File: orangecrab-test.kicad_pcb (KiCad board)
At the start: 2 copper layers, 45.7 x 58.4 mm, 27 parts, among them J1 Conn_01x16, J2 Conn_01x12, SW1 SW_Push, U1 DAC53608RTET, U2 MCP23S08T-E-ML

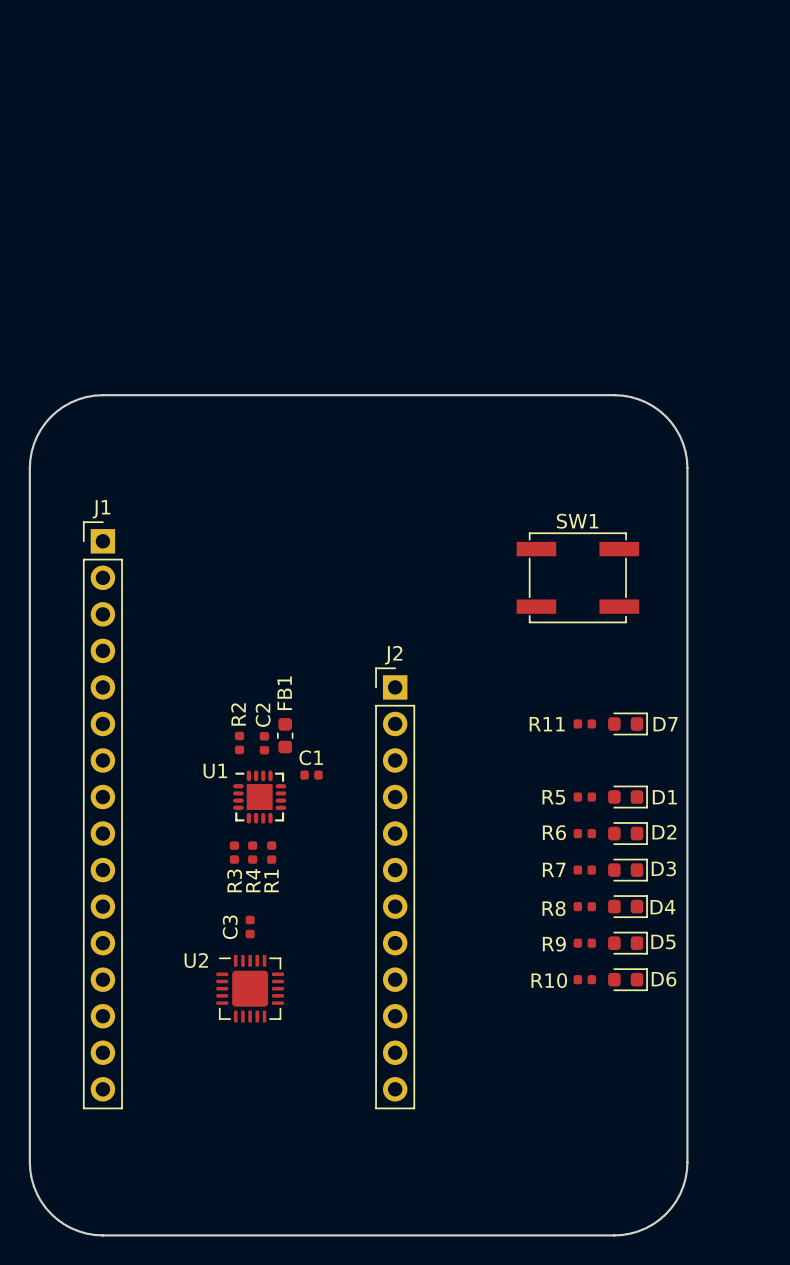
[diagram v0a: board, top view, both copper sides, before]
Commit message: Add FTDI from programming the initial firmware
Signed-off-by: Michael Welling <mwelling@ieee.org>
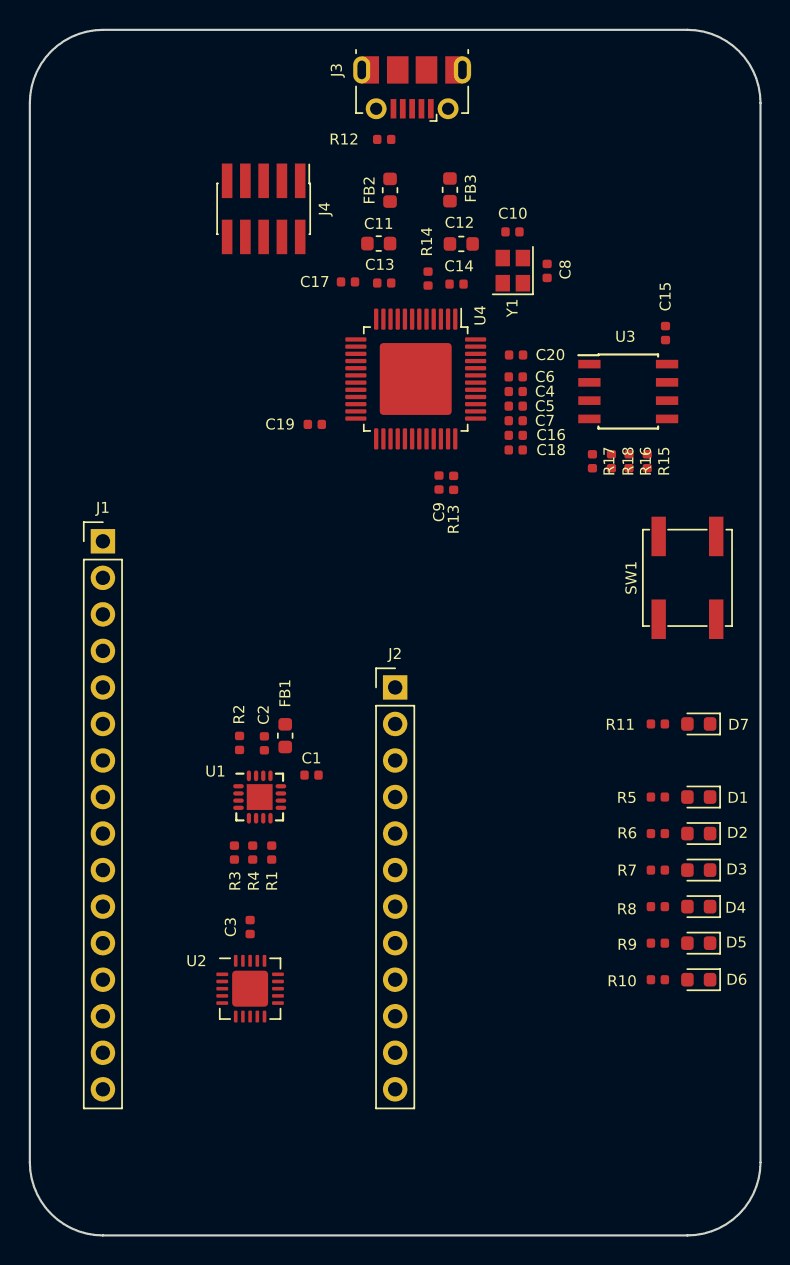
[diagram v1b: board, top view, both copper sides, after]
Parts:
- added C10: 10pF, Capacitor_SMD:C_0402_1005Metric, F.Cu at (130.1, 42.0)
- added C11: 4.7uF, Capacitor_SMD:C_0603_1608Metric, F.Cu at (120.8, 42.8)
- added C12: 4.7uF, Capacitor_SMD:C_0603_1608Metric, F.Cu at (126.5, 42.8)
- added C13: .1uF, Capacitor_SMD:C_0402_1005Metric, F.Cu at (121.2, 45.5)
- added C14: .1uF, Capacitor_SMD:C_0402_1005Metric, F.Cu at (126.2, 45.6)
- added C15: .1uF, Capacitor_SMD:C_0402_1005Metric, F.Cu at (140.7, 49.0)
- added C16: .1uF, Capacitor_SMD:C_0402_1005Metric, F.Cu at (130.3, 56.1)
- added C17: .1uF, Capacitor_SMD:C_0402_1005Metric, F.Cu at (118.6, 45.5)
- added C18: .1uF, Capacitor_SMD:C_0402_1005Metric, F.Cu at (130.3, 57.1)
- added C19: .1uF, Capacitor_SMD:C_0402_1005Metric, F.Cu at (116.3, 55.4)
- added C20: .1uF, Capacitor_SMD:C_0402_1005Metric, F.Cu at (130.3, 50.5)
- added C4: 4.7uF, Capacitor_SMD:C_0402_1005Metric, F.Cu at (130.3, 53.1)
- added C5: 4.7uF, Capacitor_SMD:C_0402_1005Metric, F.Cu at (130.3, 54.1)
- added C6: .1uF, Capacitor_SMD:C_0402_1005Metric, F.Cu at (130.3, 52.1)
- added C7: .1uF, Capacitor_SMD:C_0402_1005Metric, F.Cu at (130.3, 55.1)
- added C8: 10pF, Capacitor_SMD:C_0402_1005Metric, F.Cu at (132.5, 44.7)
- added C9: 10nF, Capacitor_SMD:C_0402_1005Metric, F.Cu at (125.0, 59.4)
- added FB2: Ferrite_Bead_Small, Inductor_SMD:L_0603_1608Metric, F.Cu at (121.6, 39.1)
- added FB3: Ferrite_Bead_Small, Inductor_SMD:L_0603_1608Metric, F.Cu at (125.7, 39.1)
- added J3: USB_B_Micro, Connector_USB:USB_Micro-B_Molex-105017-0001, F.Cu at (123.1, 32.0)
- added J4: JTAG, Connector_PinHeader_1.27mm:PinHeader_2x05_P1.27mm_Vertical_SMD, F.Cu at (112.8, 40.4)
- added R12: 1M, Resistor_SMD:R_0402_1005Metric, F.Cu at (121.2, 35.6)
- added R13: 4.7K, Resistor_SMD:R_0402_1005Metric, F.Cu at (126.0, 59.4)
- added R14: 12K, Resistor_SMD:R_0402_1005Metric, F.Cu at (124.2, 45.2)
- added R15: 4.7K, Resistor_SMD:R_0402_1005Metric, F.Cu at (139.4, 57.9)
- added R16: 4.7K, Resistor_SMD:R_0402_1005Metric, F.Cu at (138.2, 57.9)
- added R17: 2.2K, Resistor_SMD:R_0402_1005Metric, F.Cu at (135.6, 57.9)
- added R18: 4.7K, Resistor_SMD:R_0402_1005Metric, F.Cu at (137.0, 57.9)
- added U3: 93C46B/SN, Package_SO:SOIC-8_3.9x4.9mm_P1.27mm, F.Cu at (138.1, 53.1)
- added U4: FT232HL-REEL, Package_QFP:TQFP-48-1EP_7x7mm_P0.5mm_EP5x5mm, F.Cu at (123.3, 52.2)
- added Y1: 12MHz, Crystal:Crystal_SMD_2520-4Pin_2.5x2.0mm, F.Cu at (130.1, 44.7)
- moved SW1 7.62 mm to (142.2, 66.0), turned to 90 degrees
- moved D1 5.08 mm to (143.0, 81.3)
- moved D2 5.08 mm to (143.0, 83.8)
- moved D3 5.08 mm to (143.0, 86.4)
- moved D4 5.08 mm to (143.0, 88.9)
- moved D5 5.08 mm to (143.0, 91.4)
- moved D6 5.08 mm to (143.0, 94.0)
- moved D7 5.08 mm to (143.0, 76.2)
- moved R10 5.08 mm to (140.2, 94.0)
- moved R11 5.08 mm to (140.2, 76.2)
- moved R5 5.08 mm to (140.2, 81.3)
- moved R6 5.08 mm to (140.2, 83.8)
- moved R7 5.08 mm to (140.2, 86.4)
- moved R8 5.08 mm to (140.2, 88.9)
- moved R9 5.08 mm to (140.2, 91.4)
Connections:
- U2 pad 10: /IO_12 -> /IO_9
- U2 pad 11: /IO_11 -> /IO_10
- U2 pad 12: /IO_10 -> /IO_11
- U2 pad 13: /IO_9 -> /IO_12
- U2 pad 14: /IO_6 -> /IO_13
- U2 pad 9: /IO_13 -> /IO_6
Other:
- board size 45.7 x 58.4 mm -> 50.8 x 83.8 mm

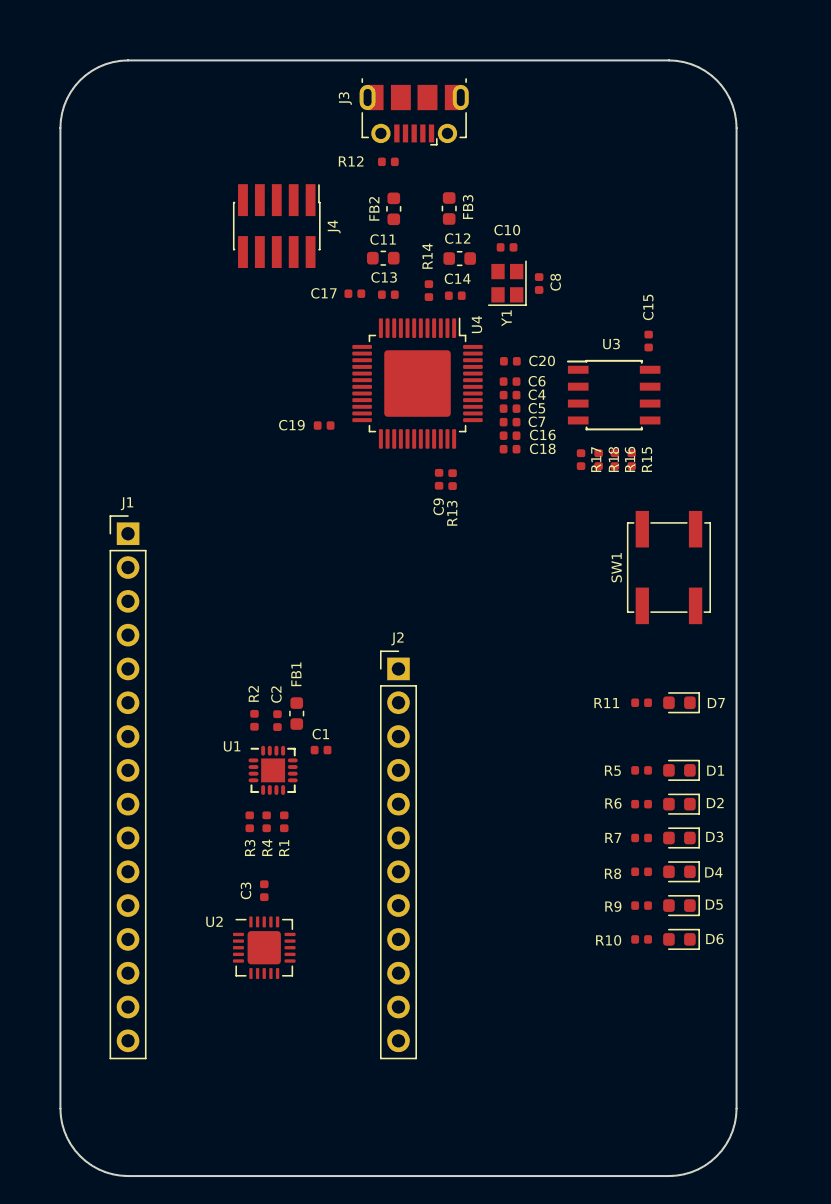
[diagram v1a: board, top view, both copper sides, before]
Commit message: Route board
Consider making the FTDI a snap off section.

Signed-off-by: Michael Welling <mwelling@ieee.org>
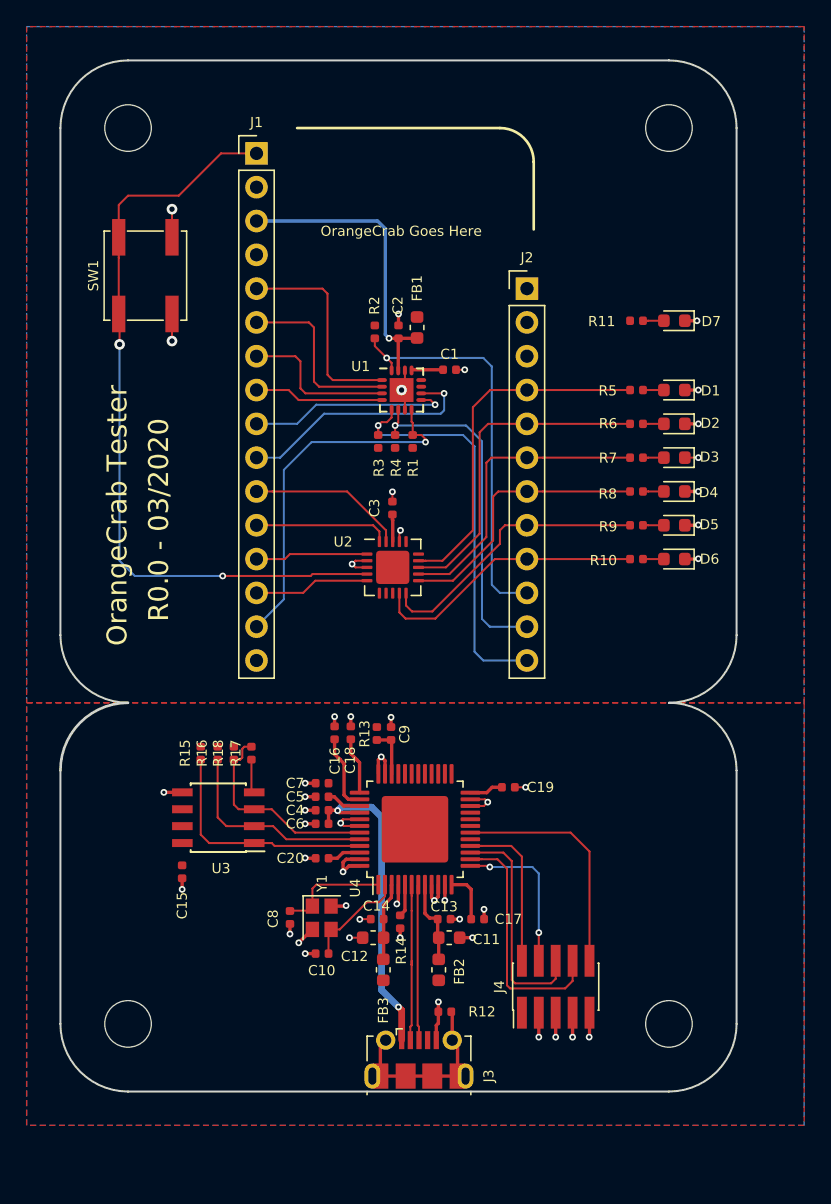
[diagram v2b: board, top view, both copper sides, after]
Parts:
- added H1: MountingHole, MountingHole:MountingHole_3.5mm, F.Cu at (101.6, 33.0)
- added H2: MountingHole, MountingHole:MountingHole_3.5mm, F.Cu at (142.2, 33.0)
- added H3: MountingHole, MountingHole:MountingHole_3.5mm, F.Cu at (101.6, 100.3)
- added H4: MountingHole, MountingHole:MountingHole_3.5mm, F.Cu at (142.2, 100.3)
- moved J3 71.0 mm to (123.5, 103.0), turned to 0 degrees
- moved R12 64.0 mm to (125.4, 99.4), turned to 180 degrees
- moved J4 60.9 mm to (133.7, 97.5), turned to 90 degrees
- moved FB3 57.4 mm to (120.8, 96.3), turned to 270 degrees
- moved FB2 57.3 mm to (124.9, 96.3), turned to 270 degrees
- moved C10 54.9 mm to (116.2, 95.0), turned to 180 degrees
- moved C15 53.1 mm to (105.7, 88.9), turned to 270 degrees
- moved C12 51.4 mm to (120.0, 93.9), turned to 180 degrees
- moved C11 51.3 mm to (125.7, 93.9), turned to 0 degrees
- moved C8 51.2 mm to (113.8, 92.3), turned to 270 degrees
- moved Y1 49.7 mm to (116.2, 92.4), turned to 270 degrees
- moved C17 47.9 mm to (127.9, 92.5), turned to 0 degrees
- moved R14 47.5 mm to (122.0, 92.7), turned to 90 degrees
- moved C14 47.2 mm to (120.3, 92.5), turned to 180 degrees
- moved C13 47.1 mm to (125.3, 92.5), turned to 0 degrees
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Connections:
- C15 pad 1: +3V3 -> Net-(C15-Pad1)
- C17 pad 1: +3V3 -> +3.3VA
- C19 pad 1: +3V3 -> +3.3VA
- C20 pad 1: +3V3 -> +3.3VA
- C5 pad 1: +3V3 -> +3.3VA
- C7 pad 1: +3V3 -> +3.3VA
- FB2 pad 2: +3V3 -> +3.3VA
- FB3 pad 2: +3V3 -> +3.3VA
- J4 pad 1: +3V3 -> Net-(J4-Pad1)
- R13 pad 2: +3V3 -> +3.3VA
- R15 pad 2: +3V3 -> +3.3VA
- R16 pad 2: +3V3 -> +3.3VA
- R18 pad 2: +3V3 -> +3.3VA
- U3 pad 8: +3V3 -> Net-(C15-Pad1)
- U4 pad 12: +3V3 -> +3.3VA
- U4 pad 24: +3V3 -> +3.3VA
- U4 pad 39: +3V3 -> +3.3VA
- U4 pad 46: +3V3 -> +3.3VA
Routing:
- net GND: track 0.00 -> 66.3 mm, vias 0 -> 48
- net /RESET: track 0.00 -> 57.8 mm, vias 0 -> 2
- net /~CLR_IO5: track 0.00 -> 30.4 mm, vias 0 -> 1
- net /SDA: track 0.00 -> 30.3 mm, vias 0 -> 1
- net /~LDAC_IO0: track 0.00 -> 27.4 mm, vias 0 -> 1
- net /IO_13: track 0.00 -> 26.6 mm
- net /SCL: track 0.00 -> 26.0 mm, vias 0 -> 1
- net /IO_12: track 0.00 -> 24.8 mm
- net +5V: track 0.00 -> 24.5 mm, vias 0 -> 2
- net /AREF: track 0.00 -> 22.8 mm, vias 0 -> 1
- net /IO_11: track 0.00 -> 22.8 mm
- net /IO_9: track 0.00 -> 21.2 mm
- net /IO_6: track 0.00 -> 20.8 mm
- net /IO_10: track 0.00 -> 20.6 mm
- net /JTAG_TDI: track 0.00 -> 18.6 mm
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- added copper zone on F.Cu, net +3.3VA
- added copper zone on F.Cu, net +3V3
- added copper zone on B.Cu, net GND
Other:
- board size 50.8 x 83.8 mm -> 50.8 x 77.5 mm
- net class Default: clearance 0.2 -> 0.1524; trace_width 0.25 -> 0.1524; via_dia 0.8 -> 0.508; via_drill 0.4 -> 0.254
- rule trace_clearance: 0.2 -> 0.1524
- rule trace_min: 0.2 -> 0.1524
- rule via_min_drill: 0.3 -> 0.254
- rule via_min_size: 0.4 -> 0.508
- board text added: "OrangeCrab Goes Here"
- board text added: "OrangeCrab Tester"
- board text added: "R0.0 - 03/2020"

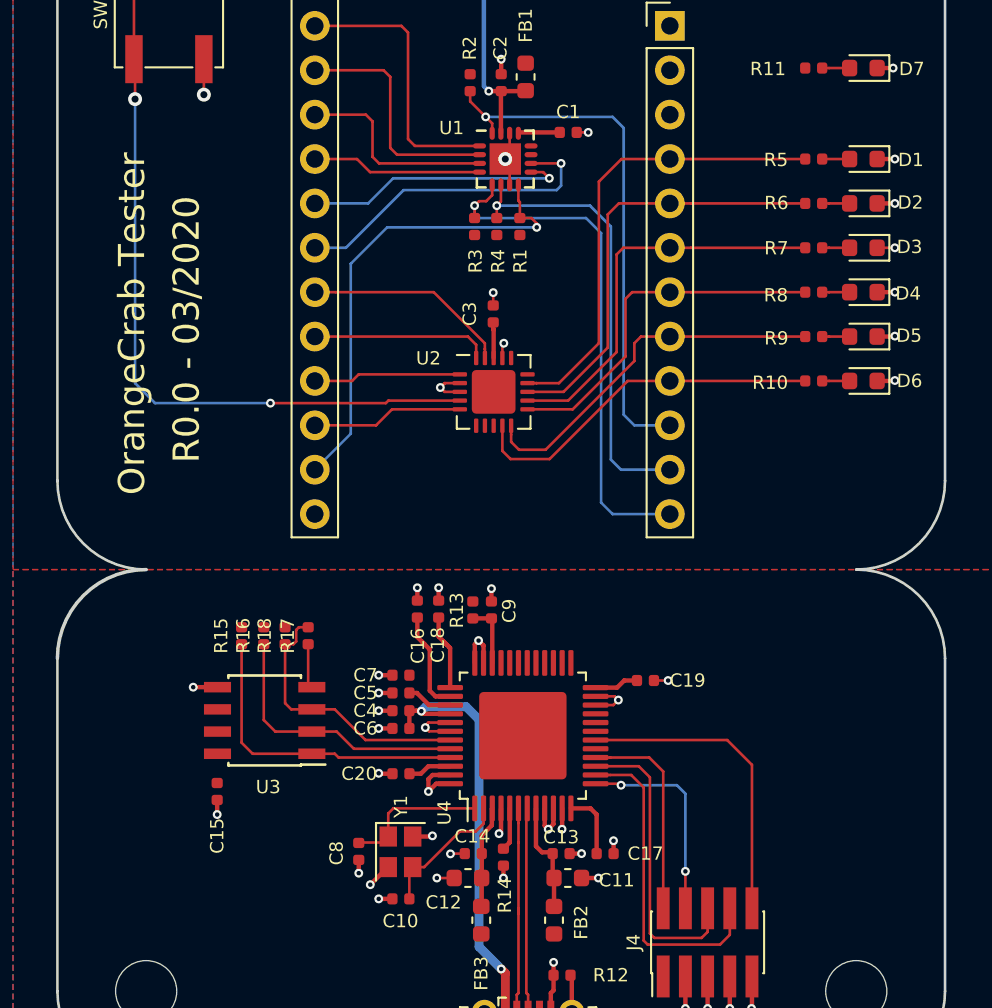
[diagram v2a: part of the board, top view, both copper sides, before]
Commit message: Add a few more mounting holes
Signed-off-by: Michael Welling <mwelling@ieee.org>
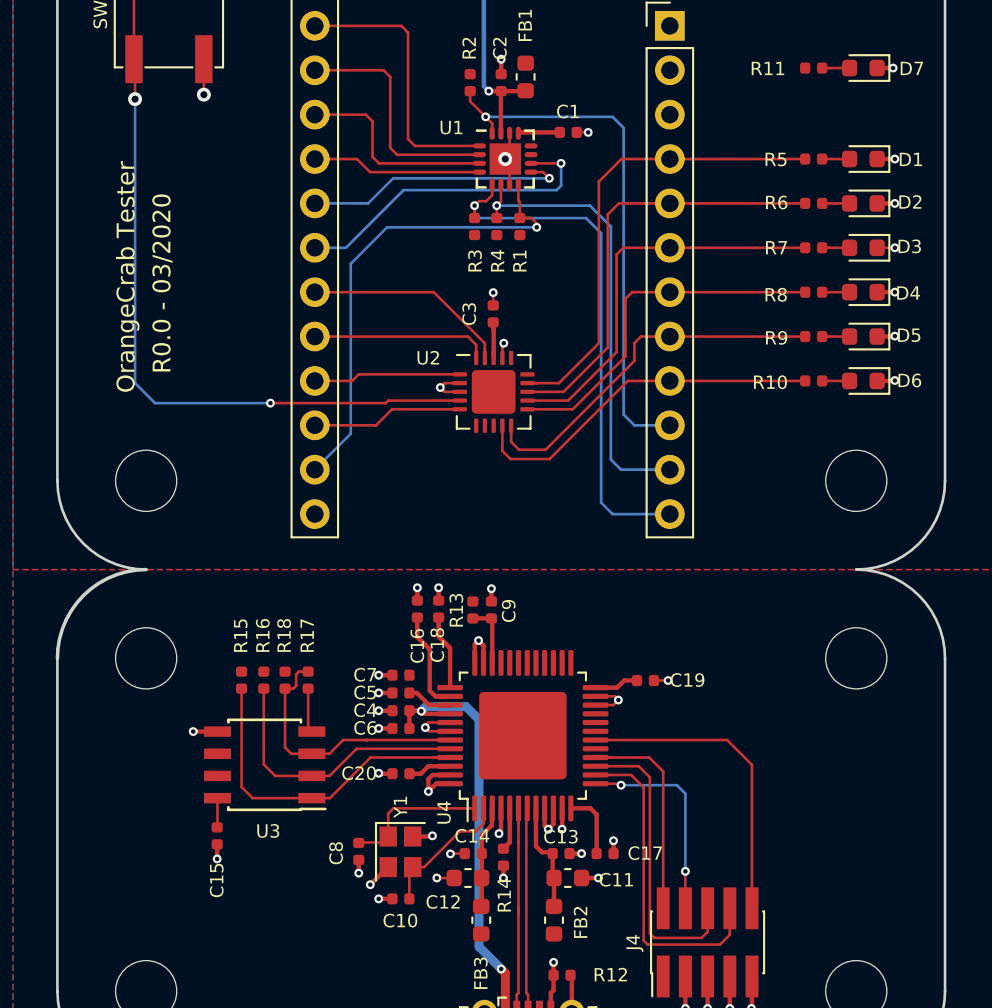
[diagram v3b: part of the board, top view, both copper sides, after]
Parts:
- added H5: MountingHole, MountingHole:MountingHole_3.5mm, F.Cu at (142.2, 71.1)
- added H6: MountingHole, MountingHole:MountingHole_3.5mm, F.Cu at (101.6, 71.1)
- added H7: MountingHole, MountingHole:MountingHole_3.5mm, F.Cu at (142.2, 81.3)
- added H8: MountingHole, MountingHole:MountingHole_3.5mm, F.Cu at (101.6, 81.3)
- moved R15 2.54 mm to (107.1, 82.5)
- moved R16 2.54 mm to (108.3, 82.5)
- moved R17 2.54 mm to (110.9, 82.5)
- moved R18 2.54 mm to (109.6, 82.5)
- moved U3 2.54 mm to (108.4, 87.4)
- moved C15 2.54 mm to (105.7, 91.4)
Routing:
- net Net-(C15-Pad1): track 0.00 -> 1.68 mm
- net /EECS: track 17.9 -> 18.8 mm
